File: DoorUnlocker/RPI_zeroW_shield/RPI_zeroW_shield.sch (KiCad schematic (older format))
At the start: 11 parts, among them J1 Conn_01x02_Male, J2 Conn_01x06_Male, J3 ServoConn, J4 ReedConn, J5 ButtonConn, K1 SANYOU_SRD_Form_C, Q1 BC547

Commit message: pcb updates
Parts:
- removed J1: Conn_01x02_Male, CustomFP:PinHeader_1x02_P2.54mm_Horizontal, symbol Connector:Conn_01x02_Male
- added J1: Conn_01x05_Male, Connector_PinHeader_2.54mm:PinHeader_1x05_P2.54mm_Vertical, symbol Connector:Conn_01x05_Male
- J2: footprint CustomFP:PinHeader_1x06_P2.54mm_Horizontal -> Connector_PinHeader_2.54mm:PinHeader_1x06_P2.54mm_Vertical
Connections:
- net 5v_IN: now also J1.1 (Pin_1)
- net GND: no longer K1.4
- net ServoPWM_P2: no longer names the net of J2.2 (Pin_2)
- net ServoPWM_P2: no longer J3.3 (Pin_3)
- new net ServoPWM_P18: J1.5 (Pin_5), J3.3 (Pin_3)
- no-connect marks 1 -> 5
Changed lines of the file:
@@
 Text Label 6450 4350 2    50   ~ 0
 3V3_IN
-Text Label 3100 1550 3    50   ~ 0
-ServoPWM_P2
+Text Label 2400 1550 3    50   ~ 0
+ServoPWM_P18
 Text Label 3200 1550 3    50   ~ 0
 Relay_P3
@@
 	0    1    1    0
 $EndComp
+Wire Wire Line
+	3900 4050 4500 4050
+Text Label 4500 4150 2    50   ~ 0
+ServoPWM_P18
+$Comp
+L Transistor_BJT:BC547 Q1
+U 1 1 5BF58CF5
+P 4350 3500
+F 0 "Q1" H 4541 3546 50  0000 L CNN
+F 1 "BC547" H 4541 3455 50  0000 L CNN
+F 2 "Package_TO_SOT_THT:TO-92_Inline" H 4550 3425 50  0001 L CIN
+F 3 "http://www.fairchildsemi.com/ds/BC/BC547.pdf" H 4350 3500 50  0001 L CNN
+	1    4350 3500
+	-1   0    0    1
+$EndComp
+$Comp
+L Device:R R1
+U 1 1 5BF58D69
+P 4700 3500
+F 0 "R1" V 4493 3500 50  0000 C CNN
+F 1 "R" V 4584 3500 50  0000 C CNN
+F 2 "Resistors:1206" V 4630 3500 50  0001 C CNN
+F 3 "~" H 4700 3500 50  0001 C CNN
+	1    4700 3500
+	0    -1   -1   0
+$EndComp
+Text Label 4850 3500 0    50   ~ 0
+Relay_P3
+Text Label 3300 4150 2    50   ~ 0
+5v_IN
+$Comp
+L power:GND #PWR02
+U 1 1 5BF58F0E
+P 4250 3300
+F 0 "#PWR02" H 4250 3050 50  0001 C CNN
+F 1 "GND" H 4255 3127 50  0000 C CNN
+F 2 "" H 4250 3300 50  0001 C CNN
+F 3 "" H 4250 3300 50  0001 C CNN
+	1    4250 3300
+	-1   0    0    1
+$EndComp
+$Comp
+L pspice:DIODE D1
+U 1 1 5BF58F4E
+P 3600 3150
+F 0 "D1" H 3600 3415 50  0000 C CNN
+F 1 "DIODE" H 3600 3324 50  0000 C CNN
+F 2 "Diode_SMD:D_SOD-323_HandSoldering" H 3600 3150 50  0001 C CNN
+F 3 "~" H 3600 3150 50  0001 C CNN
+	1    3600 3150
+	-1   0    0    1
+$EndComp
+Wire Wire Line
+	3400 3150 3300 3150
+Wire Wire Line
+	3300 3150 3300 3750
+Wire Wire Line
+	3800 3150 3900 3150
+Wire Wire Line
+	3900 3150 3900 3750
+Text Label 3300 3750 2    50   ~ 0
+5v_IN
+Wire Notes Line
+	1800 1100 3800 1100
+Wire Notes Line
+	3800 1100 3800 2100
+Wire Notes Line
+	3800 2100 1800 2100
+Wire Notes Line
+	1800 2100 1800 1100
+Wire Notes Line
+	5950 5000 7050 5000
+Wire Notes Line
+	7050 5000 7050 4100
+Wire Notes Line
+	7050 4100 5950 4100
+Wire Notes Line
+	5950 4100 5950 5000
+Wire Notes Line
+	1800 2700 1800 4600
+Wire Notes Line
+	1800 4600 4700 4600
+Wire Notes Line
+	4700 4600 4700 2700
+Wire Notes Line
+	4700 2700 1800 2700
+Text Notes 1900 3050 0    200  ~ 0
+Servo
+Text Notes 6250 4200 0    100  ~ 0
+Button
+Text Notes 2550 1250 0    100  ~ 0
+Inputs
+Text Label 6350 2600 2    50   ~ 0
+3V3_IN
+$Comp
+L Connector:Conn_01x02_Female J4
+U 1 1 5BF598EB
+P 6550 2600
+F 0 "J4" H 6577 2576 50  0000 L CNN
+F 1 "ReedConn" H 6577 2485 50  0000 L CNN
+F 2 "CustomFP:PinHeader_1x02_P2.54mm_Horizontal" H 6550 2600 50  0001 C CNN
+F 3 "~" H 6550 2600 50  0001 C CNN
+	1    6550 2600
+	1    0    0    -1
+$EndComp
+$Comp
+L Device:R R2
+U 1 1 5BF598F1
+P 6350 2850
+F 0 "R2" H 6420 2896 50  0000 L CNN
+F 1 "R" H 6420 2805 50  0000 L CNN
+F 2 "Resistors:1206" V 6280 2850 50  0001 C CNN
+F 3 "~" H 6350 2850 50  0001 C CNN
+	1    6350 2850
+	1    0    0    -1
+$EndComp
+$Comp
+L power:GND #PWR06
+U 1 1 5BF598F7
+P 6350 3000
+F 0 "#PWR06" H 6350 2750 50  0001 C CNN
+F 1 "GND" H 6355 2827 50  0000 C CNN
+F 2 "" H 6350 3000 50  0001 C CNN
+F 3 "" H 6350 3000 50  0001 C CNN
+	1    6350 3000
+	1    0    0    -1
+$EndComp
+Wire Notes Line
+	5850 3250 6950 3250
+Wire Notes Line
+	6950 3250 6950 2350
+Wire Notes Line
+	6950 2350 5850 2350
+Wire Notes Line
+	5850 2350 5850 3250
+Text Notes 6150 2450 0    100  ~ 0
+Reed
+Text Label 6350 2700 2    50   ~ 0
+Reed_P17
+$Comp
+L Connector:Conn_01x06_Male J2
+U 1 1 5BF5D2C2
+P 3200 1350
+F 0 "J2" V 3260 963 50  0000 R CNN
+F 1 "Conn_01x06_Male" V 3351 963 50  0000 R CNN
+F 2 "Connector_PinHeader_2.54mm:PinHeader_1x06_P2.54mm_Vertical" H 3200 1350 50  0001 C CNN
+F 3 "~" H 3200 1350 50  0001 C CNN
+	1    3200 1350
+	0    -1   1    0
+$EndComp
+Text Label 3000 1550 3    50   ~ 0
+3V3_IN
+Wire Wire Line
+	4250 3700 4250 3750
+Wire Wire Line
+	4250 3750 3900 3750
+$Comp
+L Connector:Conn_01x05_Male J1
+U 1 1 5BF51397
+P 2200 1350
+F 0 "J1" V 2260 1063 50  0000 R CNN
+F 1 "Conn_01x05_Male" V 2351 1063 50  0000 R CNN
+F 2 "Connector_PinHeader_2.54mm:PinHeader_1x05_P2.54mm_Vertical" H 2200 1350 50  0001 C CNN
+F 3 "~" H 2200 1350 50  0001 C CNN
+	1    2200 1350
+	0    -1   1    0
+$EndComp
+NoConn ~ 2100 1550
+NoConn ~ 2200 1550
+NoConn ~ 2300 1550
+NoConn ~ 3100 1550
+Connection ~ 3900 3750
 $Comp
 L Relay:SANYOU_SRD_Form_C K1
@@
 	0    1    1    0
 $EndComp
-Wire Wire Line
-	3900 4050 4500 4050
-Text Label 4500 4150 2    50   ~ 0
-ServoPWM_P2
-$Comp
-L power:GND #PWR04
-U 1 1 5BF58C84
-P 3900 4250
-F 0 "#PWR04" H 3900 4000 50  0001 C CNN
-F 1 "GND" H 3905 4077 50  0000 C CNN
-F 2 "" H 3900 4250 50  0001 C CNN
-F 3 "" H 3900 4250 50  0001 C CNN
-	1    3900 4250
-	1    0    0    -1
-$EndComp
-$Comp
-L Transistor_BJT:BC547 Q1
-U 1 1 5BF58CF5
-P 4350 3500
-F 0 "Q1" H 4541 3546 50  0000 L CNN
-F 1 "BC547" H 4541 3455 50  0000 L CNN
-F 2 "Package_TO_SOT_THT:TO-92_Inline" H 4550 3425 50  0001 L CIN
-F 3 "http://www.fairchildsemi.com/ds/BC/BC547.pdf" H 4350 3500 50  0001 L CNN
-	1    4350 3500
-	-1   0    0    1
-$EndComp
-$Comp
-L Device:R R1
-U 1 1 5BF58D69
-P 4700 3500
-F 0 "R1" V 4493 3500 50  0000 C CNN
-F 1 "R" V 4584 3500 50  0000 C CNN
-F 2 "Resistors:1206" V 4630 3500 50  0001 C CNN
-F 3 "~" H 4700 3500 50  0001 C CNN
-	1    4700 3500
-	0    -1   -1   0
-$EndComp
-Text Label 4850 3500 0    50   ~ 0
-Relay_P3
-Text Label 3300 4150 2    50   ~ 0
-5v_IN
-$Comp
-L power:GND #PWR02
-U 1 1 5BF58F0E
-P 4250 3300
-F 0 "#PWR02" H 4250 3050 50  0001 C CNN
-F 1 "GND" H 4255 3127 50  0000 C CNN
-F 2 "" H 4250 3300 50  0001 C CNN
-F 3 "" H 4250 3300 50  0001 C CNN
-	1    4250 3300
-	-1   0    0    1
-$EndComp
-$Comp
-L pspice:DIODE D1
-U 1 1 5BF58F4E
-P 3600 3150
-F 0 "D1" H 3600 3415 50  0000 C CNN
-F 1 "DIODE" H 3600 3324 50  0000 C CNN
-F 2 "Diode_SMD:D_SOD-323_HandSoldering" H 3600 3150 50  0001 C CNN
-F 3 "~" H 3600 3150 50  0001 C CNN
-	1    3600 3150
-	-1   0    0    1
-$EndComp
-Wire Wire Line
-	3400 3150 3300 3150
-Wire Wire Line
-	3300 3150 3300 3750
-Wire Wire Line
-	3800 3150 3900 3150
-Wire Wire Line
-	3900 3150 3900 3750
-Text Label 3300 3750 2    50   ~ 0
-5v_IN
-Wire Notes Line
-	1800 1100 3800 1100
-Wire Notes Line
-	3800 1100 3800 2100
-Wire Notes Line
-	3800 2100 1800 2100
-Wire Notes Line
-	1800 2100 1800 1100
-Wire Notes Line
-	5950 5000 7050 5000
-Wire Notes Line
-	7050 5000 7050 4100
-Wire Notes Line
-	7050 4100 5950 4100
-Wire Notes Line
-	5950 4100 5950 5000
-Wire Notes Line
-	1800 2700 1800 4600
-Wire Notes Line
-	1800 4600 4700 4600
-Wire Notes Line
-	4700 4600 4700 2700
-Wire Notes Line
-	4700 2700 1800 2700
-Text Notes 1900 3050 0    200  ~ 0
-Servo
-Text Notes 6250 4200 0    100  ~ 0
-Button
-Text Notes 2000 2000 0    100  ~ 0
-Inputs
-Text Label 6350 2600 2    50   ~ 0
-3V3_IN
-$Comp
-L Connector:Conn_01x02_Female J4
-U 1 1 5BF598EB
-P 6550 2600
-F 0 "J4" H 6577 2576 50  0000 L CNN
-F 1 "ReedConn" H 6577 2485 50  0000 L CNN
-F 2 "CustomFP:PinHeader_1x02_P2.54mm_Horizontal" H 6550 2600 50  0001 C CNN
-F 3 "~" H 6550 2600 50  0001 C CNN
-	1    6550 2600
-	1    0    0    -1
-$EndComp
-$Comp
-L Device:R R2
-U 1 1 5BF598F1
-P 6350 2850
-F 0 "R2" H 6420 2896 50  0000 L CNN
-F 1 "R" H 6420 2805 50  0000 L CNN
-F 2 "Resistors:1206" V 6280 2850 50  0001 C CNN
-F 3 "~" H 6350 2850 50  0001 C CNN
-	1    6350 2850
-	1    0    0    -1
-$EndComp
-$Comp
-L power:GND #PWR06
-U 1 1 5BF598F7
-P 6350 3000
-F 0 "#PWR06" H 6350 2750 50  0001 C CNN
-F 1 "GND" H 6355 2827 50  0000 C CNN
-F 2 "" H 6350 3000 50  0001 C CNN
-F 3 "" H 6350 3000 50  0001 C CNN
-	1    6350 3000
-	1    0    0    -1
-$EndComp
-Wire Notes Line
-	5850 3250 6950 3250
-Wire Notes Line
-	6950 3250 6950 2350
-Wire Notes Line
-	6950 2350 5850 2350
-Wire Notes Line
-	5850 2350 5850 3250
-Text Notes 6150 2450 0    100  ~ 0
-Reed
-Text Label 6350 2700 2    50   ~ 0
-Reed_P17
-$Comp
-L Connector:Conn_01x02_Male J1
-U 1 1 5BF5CF9F
-P 2000 1350
-F 0 "J1" V 2060 1163 50  0000 R CNN
-F 1 "Conn_01x02_Male" V 2151 1163 50  0000 R CNN
-F 2 "CustomFP:PinHeader_1x02_P2.54mm_Horizontal" H 2000 1350 50  0001 C CNN
-F 3 "~" H 2000 1350 50  0001 C CNN
-	1    2000 1350
-	0    -1   1    0
-$EndComp
-$Comp
-L Connector:Conn_01x06_Male J2
-U 1 1 5BF5D2C2
-P 3200 1350
-F 0 "J2" V 3260 963 50  0000 R CNN
-F 1 "Conn_01x06_Male" V 3351 963 50  0000 R CNN
-F 2 "CustomFP:PinHeader_1x06_P2.54mm_Horizontal" H 3200 1350 50  0001 C CNN
-F 3 "~" H 3200 1350 50  0001 C CNN
-	1    3200 1350
-	0    -1   1    0
-$EndComp
-Text Label 3000 1550 3    50   ~ 0
-3V3_IN
-Wire Wire Line
-	4250 3700 4250 3750
-Wire Wire Line
-	4250 3750 3900 3750
-Connection ~ 3900 3750
-NoConn ~ 2100 1550
+NoConn ~ 3900 4250
 $EndSCHEMATC

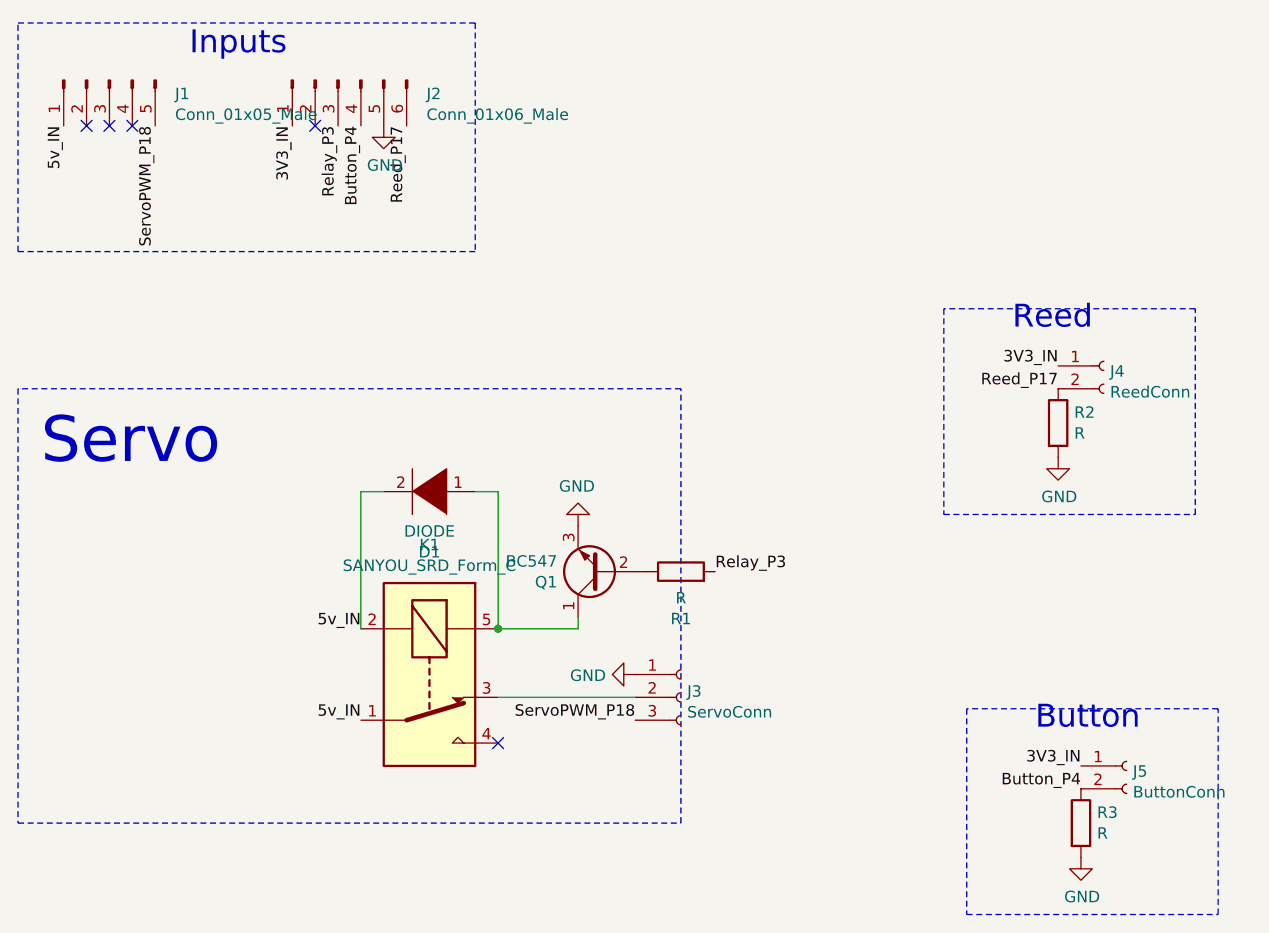
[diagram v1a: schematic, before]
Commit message: Updated Door Unlocker and PS
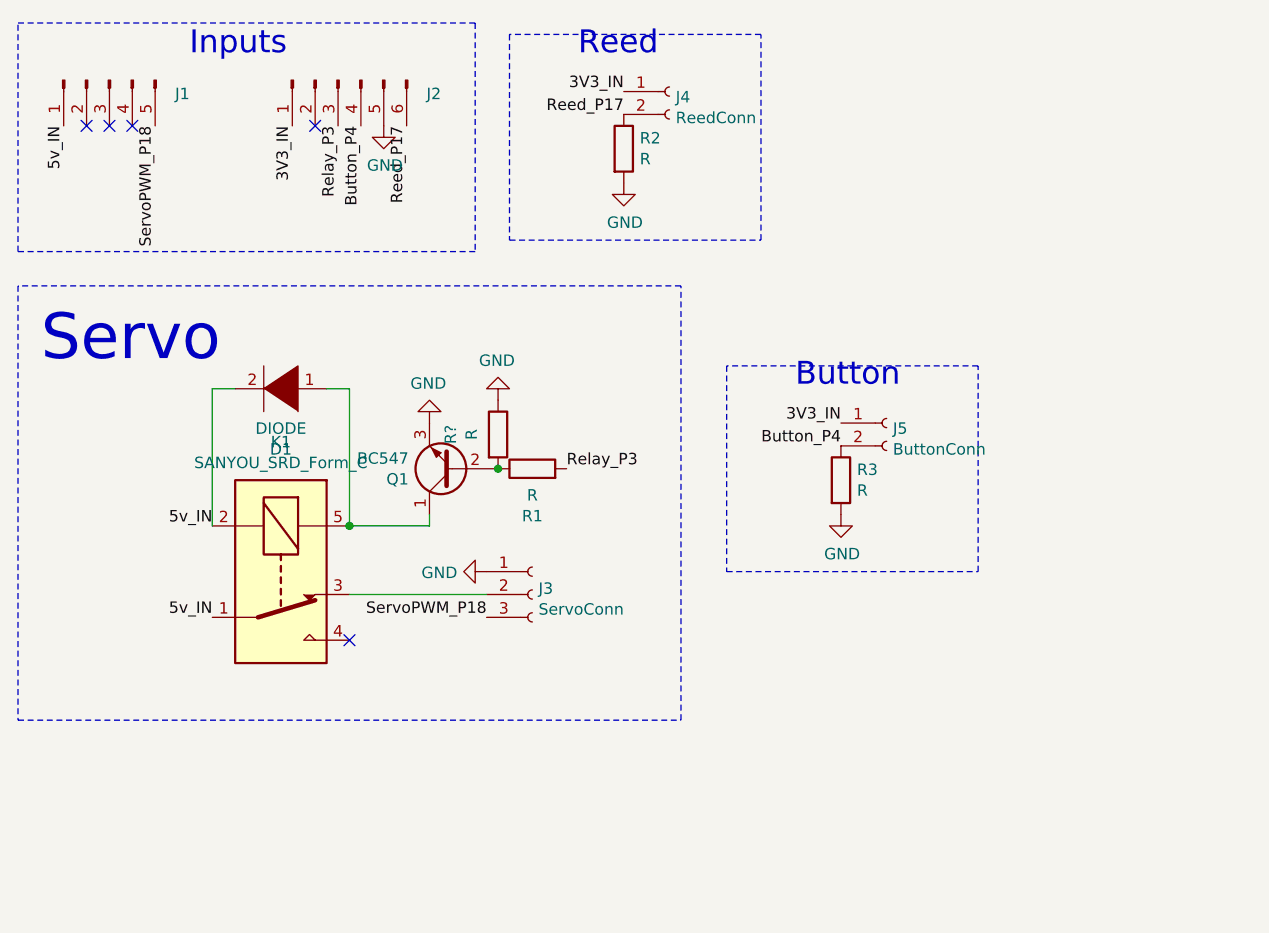
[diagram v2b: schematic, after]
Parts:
- added R?: R, Resistors:1206, symbol Device:R
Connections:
- net GND: now also R?.1
- net at Q1.2 (B), R1.1: now also R?.2
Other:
- moved on the sheet: D1, J3, J4, J5, K1, Q1, R1, R2, R3
